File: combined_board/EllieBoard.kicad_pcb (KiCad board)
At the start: 2 copper layers, 196.8 x 160.2 mm, 59 parts

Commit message: fixing net issues
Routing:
- net IO36: track 92.2 -> 97.0 mm
- net +3V3: track 553.3 -> 557.0 mm
- net GND: track 682.6 -> 684.6 mm
- net A2-: track 95.0 -> 93.6 mm
- net IO12: track 63.0 -> 64.3 mm
- net IO2: track 78.2 -> 77.1 mm
- net A6-: track 77.3 -> 78.1 mm
- net IO34: vias 0 -> 1

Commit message: PCB Added silkscreen and final review from Trevor
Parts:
- moved Servo 2 Backup 0.26 mm to (142.2, 20.1)
- moved Servo 1 Backup 0.25 mm to (106.7, 20.1)
- moved Servo 1  0.16 mm to (94.0, 20.3)
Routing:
- net GND: track 684.6 -> 630.7 mm
- net IO36: track 97.0 -> 93.4 mm
- net A2-: track 93.6 -> 90.9 mm
- net IO5: track 95.8 -> 98.3 mm
- net IO23: track 81.0 -> 83.5 mm
- net IO21: track 38.3 -> 40.8 mm
- net IO2: track 77.1 -> 79.7 mm
- net IO19: track 32.5 -> 35.1 mm
- net IO15: track 55.3 -> 57.9 mm
- net IO25: track 95.9 -> 93.4 mm
- net IO22: track 65.7 -> 68.3 mm
- net SDO/SD0: track 95.8 -> 98.0 mm
- net +3V3: track 557.0 -> 558.9 mm
- net IO39: track 114.7 -> 113.7 mm
- net IO34: track 59.5 -> 58.4 mm, vias 1 -> 0
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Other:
- board text added: "Designed by: Scout Weber & Trevor Zinky in 72 hours April 2022 Board Review: Rajiv Govindjee"
- board text added: "Experiemental Liquid Low Impulse Engine"
- board text added: "I34"
- board text added: "I35"
- board text added: "I36"
- board text added: "I39"
- board text added: "IO0"
- board text added: "IO1"
- board text added: "IO14"
- board text added: "IO15"
- board text added: "IO16"
- board text added: "IO17"
- board text added: "IO19"
- board text added: "IO2"
- board text added: "IO21"
- board text added: "IO22"
- board text added: "IO23"
- board text added: "IO25"
- board text added: "IO26"
- board text added: "IO27"
- board text added: "IO3"
- board text added: "IO32"
- board text added: "IO32 or IO4"
- board text added: "IO33"
- board text added: "IO34"
- board text added: "IO35"
- board text added: "IO36"
- board text added: "IO39"
- board text added: "IO5"
- board text added: "STAR"
- board text removed: "ELLIE"

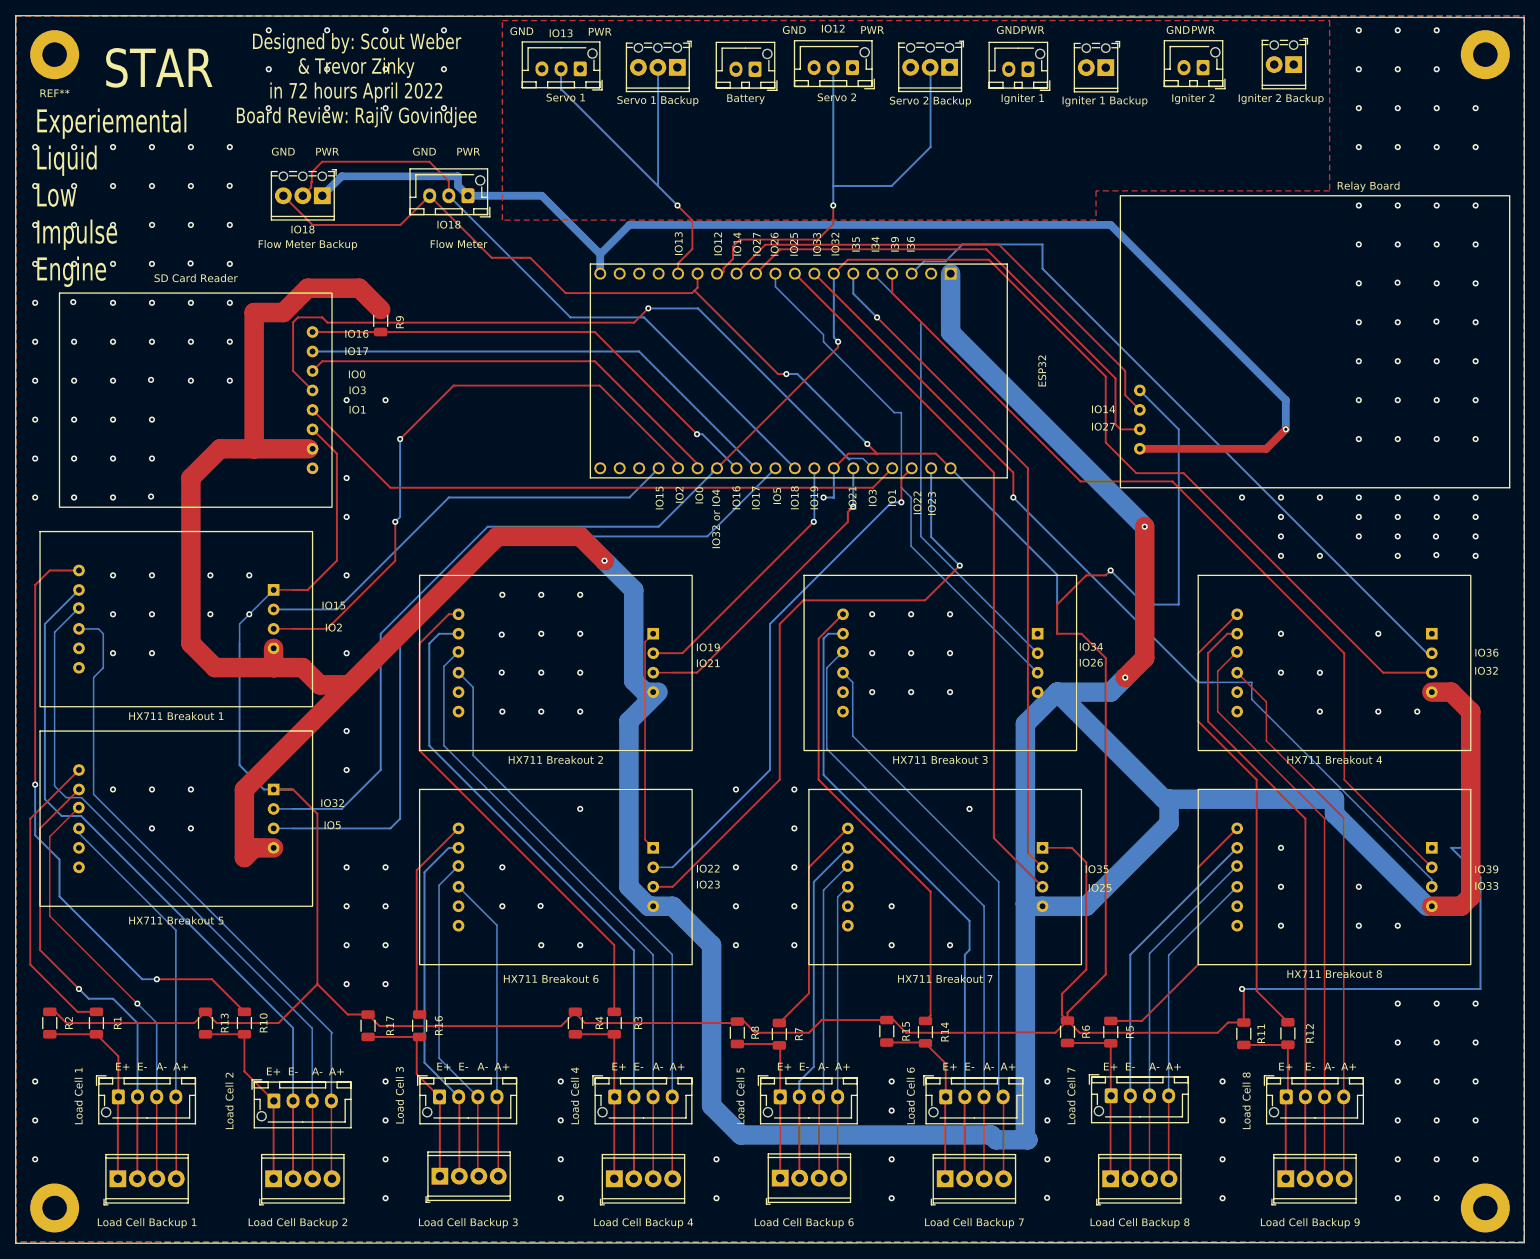
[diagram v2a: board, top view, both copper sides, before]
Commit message: Kicad board connector and silkscreen fixes
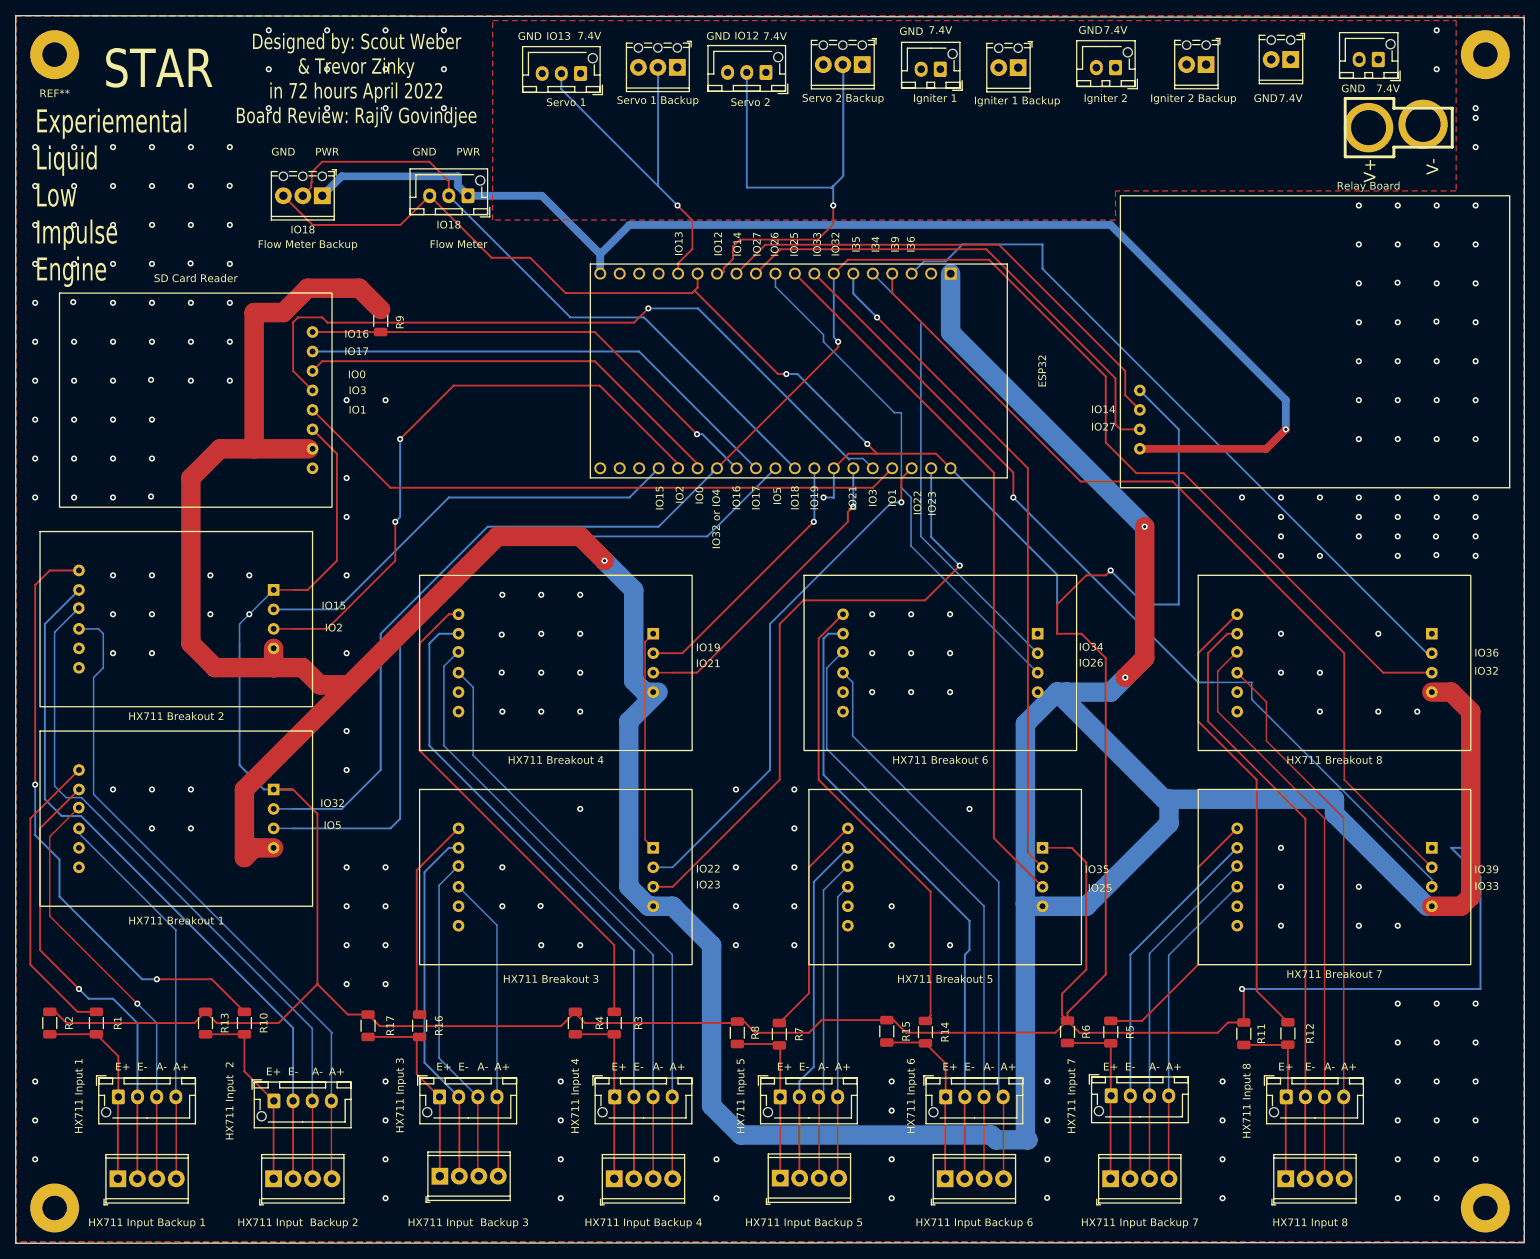
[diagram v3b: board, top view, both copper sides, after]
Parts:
- removed Battery: Battery Conn, Connector_JST:JST_XH_B2B-XH-AM_1x02_P2.50mm_Vertical
- added J10: Battery Conn Backup, Connector_JST:JST_XH_B2B-XH-AM_1x02_P2.50mm_Vertical, F.Cu at (198.1, 19.1)
- added J11: Battery Conn Backup 2, TerminalBlock_Phoenix:TerminalBlock_Phoenix_MPT-0,5-2-2.54_1x02_P2.54mm_Horizontal, F.Cu at (186.7, 19.1)
- added J9: Battery Conn, Ellie_Project_Footprints:DEANS, F.Cu at (201.4, 27.9)
- HX711 Breakout 1: renamed from HX711 Breakout 5
- HX711 Breakout 2: renamed from HX711 Breakout 1
- HX711 Breakout 3: renamed from HX711 Breakout 6
- HX711 Breakout 4: renamed from HX711 Breakout 2
- HX711 Breakout 5: renamed from HX711 Breakout 7
- HX711 Breakout 6: renamed from HX711 Breakout 3
- HX711 Breakout 7: renamed from HX711 Breakout 8
- HX711 Breakout 8: renamed from HX711 Breakout 4
- HX711 Input  2: renamed from Load Cell 2
- HX711 Input  Backup 2: renamed from Load Cell Backup 2
- HX711 Input  Backup 3: renamed from Load Cell Backup 3
- HX711 Input 1: renamed from Load Cell 1
- HX711 Input 3: renamed from Load Cell 3
- HX711 Input 4: renamed from Load Cell 4
- HX711 Input 5: renamed from Load Cell 5
- HX711 Input 6: renamed from Load Cell 6
- HX711 Input 7: renamed from Load Cell 7
- HX711 Input 8: renamed from Load Cell 8
- HX711 Input 8: renamed from Load Cell Backup 9
- HX711 Input Backup 1: renamed from Load Cell Backup 1
- HX711 Input Backup 4: renamed from Load Cell Backup 4
- HX711 Input Backup 5: renamed from Load Cell Backup 6
- HX711 Input Backup 6: renamed from Load Cell Backup 7
- HX711 Input Backup 7: renamed from Load Cell Backup 8
- moved Igniter 1  11.4 mm to (141.0, 20.3)
- moved Igniter 1 Backup 11.4 mm to (151.1, 20.1)
- moved Igniter 2 Backup 11.4 mm to (175.7, 19.7)
- moved Igniter 2  11.4 mm to (163.8, 20.1)
- moved Servo 2 Backup 11.4 mm to (130.8, 19.7)
- moved Servo 2  11.3 mm to (118.2, 20.7)
- moved Servo 1  0.61 mm to (94.0, 20.9)
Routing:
- net +3V3: track 558.9 -> 562.7 mm
- net IO12: track 64.3 -> 65.8 mm
- net IO13: track 50.0 -> 49.2 mm
- net GND: vias 261 -> 252
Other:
- board text added: "7.4V"
